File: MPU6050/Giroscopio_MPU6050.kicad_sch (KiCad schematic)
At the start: 7 parts, among them U301 MPU-6050

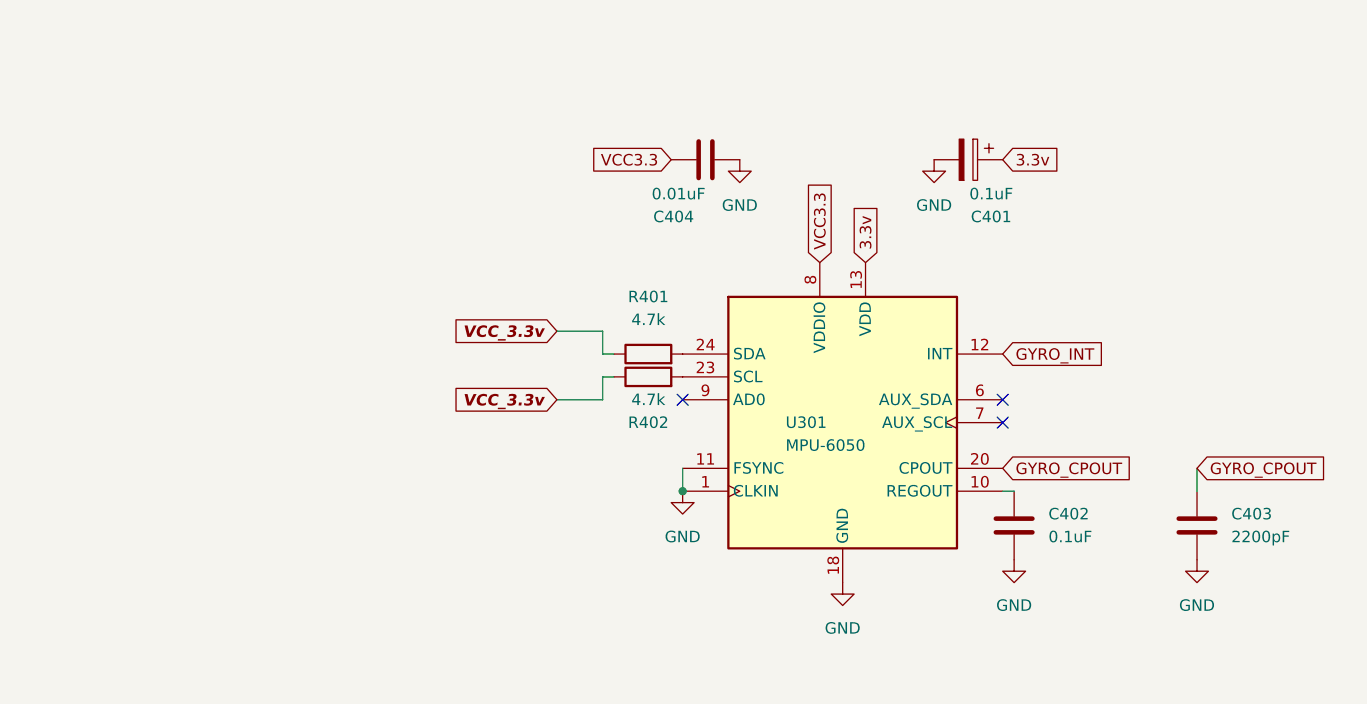
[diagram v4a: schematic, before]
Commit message: MPU6050: creazione del PCB e layout NON completo
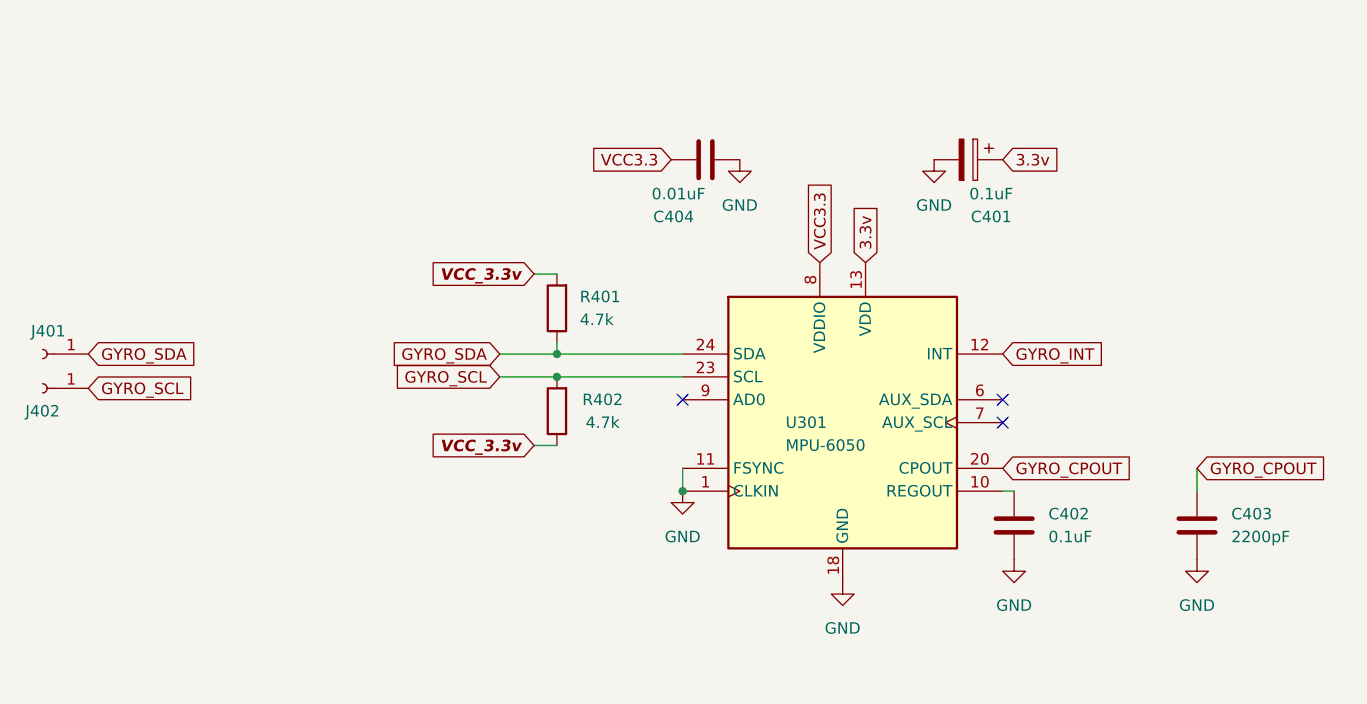
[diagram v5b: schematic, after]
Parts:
- added J401, J402: Conn_01x01_Female, TestPoint:TestPoint_Keystone_5019_Minature, symbol Connector:Conn_01x01_Female
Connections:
- net VCC_3.3v: now also R401.2; no longer R401.1
- net GYRO_SDA: now reaches U301.24 (SDA)
- net GYRO_SDA: now also R401.1, J401.1 (Pin_1); no longer R401.2
- net GYRO_SCL: now reaches R402.2, U301.23 (SCL)
- net GYRO_SCL: now also J402.1 (Pin_1)
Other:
- moved on the sheet: R401, R402
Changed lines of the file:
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@@
     (company "Vespin2")
   )
+  (junction (at 106.68 76.2) (diameter 0) (color 0 0 0 0)
+  )
   (junction (at 120.65 91.44) (diameter 0) (color 0 0 0 0)
+  )
+  (junction (at 106.68 78.74) (diameter 0) (color 0 0 0 0)
   )
   (no_connect (at 120.65 81.28))
@@
     (stroke (width 0) (type default) (color 0 0 0 0))
   )
-  (wire (pts (xy 113.03 78.74) (xy 111.76 78.74))
-    (stroke (width 0) (type default) (color 0 0 0 0))
-  )
-  (wire (pts (xy 111.76 81.28) (xy 106.68 81.28))
+  (wire (pts (xy 100.33 78.74) (xy 106.68 78.74))
     (stroke (width 0) (type default) (color 0 0 0 0))
   )
@@
     (stroke (width 0) (type default) (color 0 0 0 0))
   )
-  (wire (pts (xy 111.76 78.74) (xy 111.76 81.28))
-    (stroke (width 0) (type default) (color 0 0 0 0))
-  )
-  (wire (pts (xy 111.76 76.2) (xy 113.03 76.2))
-    (stroke (width 0) (type default) (color 0 0 0 0))
-  )
-  (wire (pts (xy 106.68 73.66) (xy 111.76 73.66))
-    (stroke (width 0) (type default) (color 0 0 0 0))
-  )
-  (wire (pts (xy 111.76 73.66) (xy 111.76 76.2))
+  (wire (pts (xy 106.68 78.74) (xy 120.65 78.74))
+    (stroke (width 0) (type default) (color 0 0 0 0))
+  )
+  (wire (pts (xy 106.68 76.2) (xy 120.65 76.2))
+    (stroke (width 0) (type default) (color 0 0 0 0))
+  )
+  (wire (pts (xy 104.14 67.31) (xy 106.68 67.31))
+    (stroke (width 0) (type default) (color 0 0 0 0))
+  )
+  (wire (pts (xy 106.68 74.93) (xy 106.68 76.2))
+    (stroke (width 0) (type default) (color 0 0 0 0))
+  )
+  (wire (pts (xy 104.14 86.36) (xy 106.68 86.36))
     (stroke (width 0) (type default) (color 0 0 0 0))
   )
@@
     (stroke (width 0) (type default) (color 0 0 0 0))
   )
+  (wire (pts (xy 100.33 76.2) (xy 106.68 76.2))
+    (stroke (width 0) (type default) (color 0 0 0 0))
+  )
   (global_label "GYRO_INT" (shape input) (at 156.21 76.2 0) (fields_autoplaced)
     (effects (font (size 1.27 1.27)) (justify left))
     (property "Intersheet References" "${INTERSHEET_REFS}" (id 0) (at 167.4526 76.1206 0)
+      (effects (font (size 1.27 1.27)) (justify left) hide)
+    )
+  )
+  (global_label "GYRO_SCL" (shape input) (at 54.61 80.01 0) (fields_autoplaced)
+    (effects (font (size 1.27 1.27)) (justify left))
+    (property "Intersheet References" "${INTERSHEET_REFS}" (id 0) (at 66.4574 80.0894 0)
       (effects (font (size 1.27 1.27)) (justify left) hide)
     )
@@
     )
   )
+  (global_label "GYRO_SDA" (shape input) (at 54.61 76.2 0) (fields_autoplaced)
+    (effects (font (size 1.27 1.27)) (justify left))
+    (property "Intersheet References" "${INTERSHEET_REFS}" (id 0) (at 66.5179 76.2794 0)
+      (effects (font (size 1.27 1.27)) (justify left) hide)
+    )
+  )
+  (global_label "GYRO_SCL" (shape input) (at 100.33 78.74 180) (fields_autoplaced)
+    (effects (font (size 1.27 1.27)) (justify right))
+    (property "Intersheet References" "${INTERSHEET_REFS}" (id 0) (at 88.4826 78.6606 0)
+      (effects (font (size 1.27 1.27)) (justify right) hide)
+    )
+  )
   (global_label "GYRO_CPOUT" (shape input) (at 177.8 88.9 0) (fields_autoplaced)
     (effects (font (size 1.27 1.27)) (justify left))
@@
     )
   )
+  (global_label "GYRO_SDA" (shape input) (at 100.33 76.2 180) (fields_autoplaced)
+    (effects (font (size 1.27 1.27)) (justify right))
+    (property "Intersheet References" "${INTERSHEET_REFS}" (id 0) (at 88.4221 76.1206 0)
+      (effects (font (size 1.27 1.27)) (justify right) hide)
+    )
+  )
   (global_label "3.3v" (shape input) (at 156.21 54.61 0) (fields_autoplaced)
     (effects (font (size 1.27 1.27)) (justify left))
@@
     )
   )
-  (global_label "VCC_3.3v" (shape input) (at 106.68 73.66 180) (fields_autoplaced)
+  (global_label "VCC_3.3v" (shape input) (at 104.14 67.31 180) (fields_autoplaced)
     (effects (font (size 1.27 1.27) (thickness 0.254) bold italic) (justify right))
-    (property "Intersheet References" "${INTERSHEET_REFS}" (id 0) (at 95.2333 73.533 0)
+    (property "Intersheet References" "${INTERSHEET_REFS}" (id 0) (at 92.6933 67.183 0)
       (effects (font (size 1.27 1.27) (thickness 0.254) bold italic) (justify right) hide)
     )
   )
-  (global_label "VCC_3.3v" (shape input) (at 106.68 81.28 180) (fields_autoplaced)
+  (global_label "VCC_3.3v" (shape input) (at 104.14 86.36 180) (fields_autoplaced)
     (effects (font (size 1.27 1.27) (thickness 0.254) bold italic) (justify right))
-    (property "Intersheet References" "${INTERSHEET_REFS}" (id 0) (at 95.2333 81.153 0)
+    (property "Intersheet References" "${INTERSHEET_REFS}" (id 0) (at 92.6933 86.233 0)
       (effects (font (size 1.27 1.27) (thickness 0.254) bold italic) (justify right) hide)
     )
@@
     (pin "2")
   )
-  (symbol (lib_id "Device:R") (at 116.84 76.2 90) (unit 1)
-    (in_bom yes) (on_board yes) (fields_autoplaced)
-    (property "Reference" "R401" (id 0) (at 116.84 69.85 90))
-    (property "Value" "4.7k" (id 1) (at 116.84 72.39 90))
-    (property "Footprint" "Resistor_SMD:R_0805_2012Metric" (id 2) (at 116.84 77.978 90)
-      (effects (font (size 1.27 1.27)) hide)
-    )
-    (property "Datasheet" "~" (id 3) (at 116.84 76.2 0)
+  (symbol (lib_id "Device:R") (at 106.68 71.12 180) (unit 1)
+    (in_bom yes) (on_board yes) (fields_autoplaced)
+    (property "Reference" "R401" (id 0) (at 109.22 69.8499 0)
+      (effects (font (size 1.27 1.27)) (justify right))
+    )
+    (property "Value" "4.7k" (id 1) (at 109.22 72.3899 0)
+      (effects (font (size 1.27 1.27)) (justify right))
+    )
+    (property "Footprint" "Resistor_SMD:R_0805_2012Metric" (id 2) (at 108.458 71.12 90)
+      (effects (font (size 1.27 1.27)) hide)
+    )
+    (property "Datasheet" "~" (id 3) (at 106.68 71.12 0)
       (effects (font (size 1.27 1.27)) hide)
     )
@@
     )
     (property "Datasheet" "" (id 3) (at 120.65 91.44 0)
+      (effects (font (size 1.27 1.27)) hide)
+    )
+    (pin "1")
+  )
+  (symbol (lib_id "Connector:Conn_01x01_Female") (at 49.53 80.01 180) (unit 1)
+    (in_bom yes) (on_board yes)
+    (property "Reference" "J402" (id 0) (at 49.53 82.55 0))
+    (property "Value" "Conn_01x01_Female" (id 1) (at 50.165 77.47 0)
+      (effects (font (size 1.27 1.27)) hide)
+    )
+    (property "Footprint" "TestPoint:TestPoint_Keystone_5019_Minature" (id 2) (at 49.53 80.01 0)
+      (effects (font (size 1.27 1.27)) hide)
+    )
+    (property "Datasheet" "~" (id 3) (at 49.53 80.01 0)
+      (effects (font (size 1.27 1.27)) hide)
+    )
+    (pin "1")
+  )
+  (symbol (lib_id "Connector:Conn_01x01_Female") (at 49.53 76.2 180) (unit 1)
+    (in_bom yes) (on_board yes) (fields_autoplaced)
+    (property "Reference" "J401" (id 0) (at 50.165 73.66 0))
+    (property "Value" "Conn_01x01_Female" (id 1) (at 50.165 73.66 0)
+      (effects (font (size 1.27 1.27)) hide)
+    )
+    (property "Footprint" "TestPoint:TestPoint_Keystone_5019_Minature" (id 2) (at 49.53 76.2 0)
+      (effects (font (size 1.27 1.27)) hide)
+    )
+    (property "Datasheet" "~" (id 3) (at 49.53 76.2 0)
       (effects (font (size 1.27 1.27)) hide)
     )
@@
     (pin "2")
   )
-  (symbol (lib_id "Device:R") (at 116.84 78.74 90) (unit 1)
+  (symbol (lib_id "Device:R") (at 106.68 82.55 180) (unit 1)
     (in_bom yes) (on_board yes)
-    (property "Reference" "R402" (id 0) (at 116.84 83.82 90))
-    (property "Value" "4.7k" (id 1) (at 116.84 81.28 90))
-    (property "Footprint" "Resistor_SMD:R_0805_2012Metric" (id 2) (at 116.84 80.518 90)
-      (effects (font (size 1.27 1.27)) hide)
-    )
-    (property "Datasheet" "~" (id 3) (at 116.84 78.74 0)
+    (property "Reference" "R402" (id 0) (at 111.76 81.28 0))
+    (property "Value" "4.7k" (id 1) (at 111.76 83.82 0))
+    (property "Footprint" "Resistor_SMD:R_0805_2012Metric" (id 2) (at 108.458 82.55 90)
+      (effects (font (size 1.27 1.27)) hide)
+    )
+    (property "Datasheet" "~" (id 3) (at 106.68 82.55 0)
       (effects (font (size 1.27 1.27)) hide)
     )
@@
       (reference "C404") (unit 1) (value "0.01uF") (footprint "Capacitor_SMD:C_0805_2012Metric")
     )
+    (path "/58845f6a-f12f-48d6-acaf-4586b4a9bbc5"
+      (reference "J401") (unit 1) (value "Conn_01x01_Female") (footprint "TestPoint:TestPoint_Keystone_5019_Minature")
+    )
+    (path "/55a46a37-a89c-4e10-9eef-3e9e38a127fb"
+      (reference "J402") (unit 1) (value "Conn_01x01_Female") (footprint "TestPoint:TestPoint_Keystone_5019_Minature")
+    )
     (path "/4a776592-badf-4679-907a-201ed16a7491"

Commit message: mpu6050: aggiunta label e testpoint
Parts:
- J401, J402: footprint TestPoint:TestPoint_Keystone_5019_Minature -> TestPoint:TestPoint_Pad_1.0x1.0mm
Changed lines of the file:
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@@
       (effects (font (size 1.27 1.27)) hide)
     )
-    (property "Footprint" "TestPoint:TestPoint_Keystone_5019_Minature" (id 2) (at 49.53 80.01 0)
+    (property "Footprint" "TestPoint:TestPoint_Pad_1.0x1.0mm" (id 2) (at 49.53 80.01 0)
       (effects (font (size 1.27 1.27)) hide)
     )
@@
       (effects (font (size 1.27 1.27)) hide)
     )
-    (property "Footprint" "TestPoint:TestPoint_Keystone_5019_Minature" (id 2) (at 49.53 76.2 0)
+    (property "Footprint" "TestPoint:TestPoint_Pad_1.0x1.0mm" (id 2) (at 49.53 76.2 0)
       (effects (font (size 1.27 1.27)) hide)
     )
@@
     )
     (path "/58845f6a-f12f-48d6-acaf-4586b4a9bbc5"
-      (reference "J401") (unit 1) (value "Conn_01x01_Female") (footprint "TestPoint:TestPoint_Keystone_5019_Minature")
+      (reference "J401") (unit 1) (value "Conn_01x01_Female") (footprint "TestPoint:TestPoint_Pad_1.0x1.0mm")
     )
     (path "/55a46a37-a89c-4e10-9eef-3e9e38a127fb"
-      (reference "J402") (unit 1) (value "Conn_01x01_Female") (footprint "TestPoint:TestPoint_Keystone_5019_Minature")
+      (reference "J402") (unit 1) (value "Conn_01x01_Female") (footprint "TestPoint:TestPoint_Pad_1.0x1.0mm")
     )
     (path "/4a776592-badf-4679-907a-201ed16a7491"

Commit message: mpu6050: aggiunta testpad
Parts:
- added J403, J404, J405: Conn_01x01_Female, TestPoint:TestPoint_Pad_1.0x1.0mm, symbol Connector:Conn_01x01_Female
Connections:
- net GND: now also J404.1 (Pin_1)
- net GYRO_INT: now also J403.1 (Pin_1)
- net VCC3.3: now also J405.1 (Pin_1)
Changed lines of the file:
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@@
+    )
+  )
+  (global_label "VCC3.3" (shape input) (at 54.61 109.22 0) (fields_autoplaced)
+    (effects (font (size 1.27 1.27)) (justify left))
+    (property "Intersheet References" "${INTERSHEET_REFS}" (id 0) (at 63.6755 109.2994 0)
+      (effects (font (size 1.27 1.27)) (justify left) hide)
     )
   )
@@
     )
   )
+  (global_label "GYRO_INT" (shape input) (at 54.61 90.17 0) (fields_autoplaced)
+    (effects (font (size 1.27 1.27)) (justify left))
+    (property "Intersheet References" "${INTERSHEET_REFS}" (id 0) (at 65.8526 90.0906 0)
+      (effects (font (size 1.27 1.27)) (justify left) hide)
+    )
+  )
   (symbol (lib_id "Device:C_Polarized") (at 152.4 54.61 270) (unit 1)
     (in_bom yes) (on_board yes)
@@
     (pin "2")
   )
+  (symbol (lib_id "Connector:Conn_01x01_Female") (at 49.53 90.17 180) (unit 1)
+    (in_bom yes) (on_board yes)
+    (property "Reference" "J403" (id 0) (at 49.53 92.71 0))
+    (property "Value" "Conn_01x01_Female" (id 1) (at 50.165 87.63 0)
+      (effects (font (size 1.27 1.27)) hide)
+    )
+    (property "Footprint" "TestPoint:TestPoint_Pad_1.0x1.0mm" (id 2) (at 49.53 90.17 0)
+      (effects (font (size 1.27 1.27)) hide)
+    )
+    (property "Datasheet" "~" (id 3) (at 49.53 90.17 0)
+      (effects (font (size 1.27 1.27)) hide)
+    )
+    (pin "1")
+  )
   (symbol (lib_id "Device:R") (at 106.68 71.12 180) (unit 1)
     (in_bom yes) (on_board yes) (fields_autoplaced)
@@
     )
     (property "Datasheet" "" (id 3) (at 148.59 54.61 0)
+      (effects (font (size 1.27 1.27)) hide)
+    )
+    (pin "1")
+  )
+  (symbol (lib_id "Connector:Conn_01x01_Female") (at 49.53 109.22 180) (unit 1)
+    (in_bom yes) (on_board yes)
+    (property "Reference" "J405" (id 0) (at 49.53 111.76 0))
+    (property "Value" "Conn_01x01_Female" (id 1) (at 50.165 106.68 0)
+      (effects (font (size 1.27 1.27)) hide)
+    )
+    (property "Footprint" "TestPoint:TestPoint_Pad_1.0x1.0mm" (id 2) (at 49.53 109.22 0)
+      (effects (font (size 1.27 1.27)) hide)
+    )
+    (property "Datasheet" "~" (id 3) (at 49.53 109.22 0)
+      (effects (font (size 1.27 1.27)) hide)
+    )
+    (pin "1")
+  )
+  (symbol (lib_id "power:GND") (at 54.61 99.06 0) (unit 1)
+    (in_bom yes) (on_board yes) (fields_autoplaced)
+    (property "Reference" "#PWR0402" (id 0) (at 54.61 105.41 0)
+      (effects (font (size 1.27 1.27)) hide)
+    )
+    (property "Value" "GND" (id 1) (at 54.61 104.14 0))
+    (property "Footprint" "" (id 2) (at 54.61 99.06 0)
+      (effects (font (size 1.27 1.27)) hide)
+    )
+    (property "Datasheet" "" (id 3) (at 54.61 99.06 0)
       (effects (font (size 1.27 1.27)) hide)
     )
@@
     (pin "1")
   )
+  (symbol (lib_id "Connector:Conn_01x01_Female") (at 49.53 99.06 180) (unit 1)
+    (in_bom yes) (on_board yes)
+    (property "Reference" "J404" (id 0) (at 49.53 101.6 0))
+    (property "Value" "Conn_01x01_Female" (id 1) (at 50.165 96.52 0)
+      (effects (font (size 1.27 1.27)) hide)
+    )
+    (property "Footprint" "TestPoint:TestPoint_Pad_1.0x1.0mm" (id 2) (at 49.53 99.06 0)
+      (effects (font (size 1.27 1.27)) hide)
+    )
+    (property "Datasheet" "~" (id 3) (at 49.53 99.06 0)
+      (effects (font (size 1.27 1.27)) hide)
+    )
+    (pin "1")
+  )
   (sheet_instances
     (path "/" (page "1"))
@@
       (reference "#PWR0401") (unit 1) (value "GND") (footprint "")
     )
+    (path "/65e5a847-e74b-436c-9186-93f1da30ff91"
+      (reference "#PWR0402") (unit 1) (value "GND") (footprint "")
+    )
     (path "/1ca5e19a-e1ad-483a-a5a7-3aaf6b67b377"
       (reference "C401") (unit 1) (value "0.1uF") (footprint "Capacitor_Tantalum_SMD:CP_EIA-1608-08_AVX-J")
@@
       (reference "J402") (unit 1) (value "Conn_01x01_Female") (footprint "TestPoint:TestPoint_Pad_1.0x1.0mm")
     )
+    (path "/20f87eb9-d308-4a5b-9e30-426e62ed56b1"
+      (reference "J403") (unit 1) (value "Conn_01x01_Female") (footprint "TestPoint:TestPoint_Pad_1.0x1.0mm")
+    )
+    (path "/ff1cef7b-e5d5-4fa0-8586-fb5a640b05c7"
+      (reference "J404") (unit 1) (value "Conn_01x01_Female") (footprint "TestPoint:TestPoint_Pad_1.0x1.0mm")
+    )
+    (path "/5da09462-4c3f-41ad-999e-13d91b5ddd7b"
+      (reference "J405") (unit 1) (value "Conn_01x01_Female") (footprint "TestPoint:TestPoint_Pad_1.0x1.0mm")
+    )
     (path "/4a776592-badf-4679-907a-201ed16a7491"
